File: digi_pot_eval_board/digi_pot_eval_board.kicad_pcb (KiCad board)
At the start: 2 copper layers, 114.3 x 163.2 mm, 85 parts, among them J1 Conn_01x07_Male, J10 Conn_01x02_Male, J11 Conn_01x02_Male, J12 Conn_01x02_Male, J13 Conn_01x06_Male, J14 Conn_01x02_Male, J2 Conn_01x10_Male, J3 USB_B, J4 Conn_01x02_Male, J7 Conn_01x02_Male, J8 DS1013-06S, J9 Conn_01x05_Male, K2 G6K2FYTR5DC, K4 G6K2FYTR5DC, K5 G6K2FYTR5DC, K6 G6K2FYTR5DC, Q1 BSS84, Q2 BSS84, SW1 SW_MEC_5G_LED, U1 DigiPot, U10 6N138, U11 NCP1117ST50T3G, U12 ATmega32U4-AU, U2 DigiPot, U3 DigiPot, U4 DigiPot, U5 DigiPot, U6 DigiPot, U7 DigiPot, U8 ULN2003A, U9 USBLC6-2SC6, Y1 16MHz HC-49SM

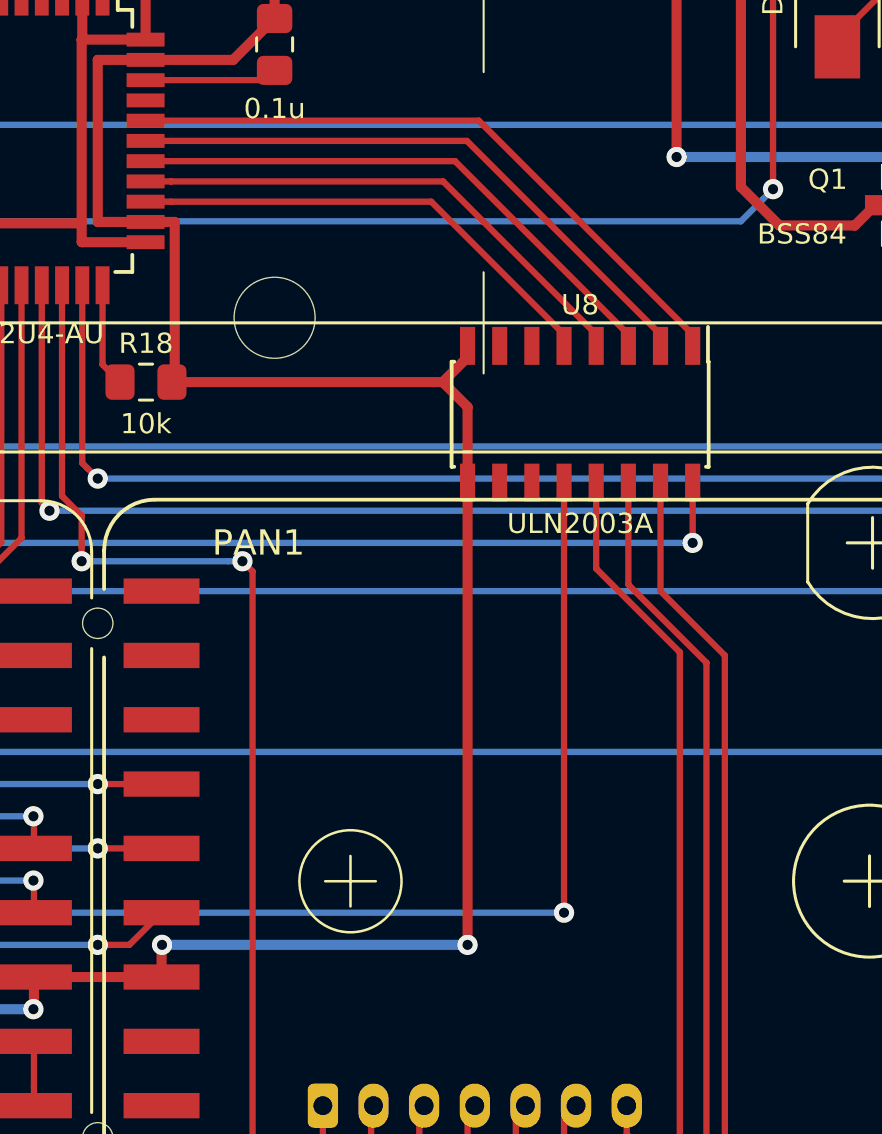
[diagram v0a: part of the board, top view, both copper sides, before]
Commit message: Upgrading KiCad and fixing ULN2003a connection.
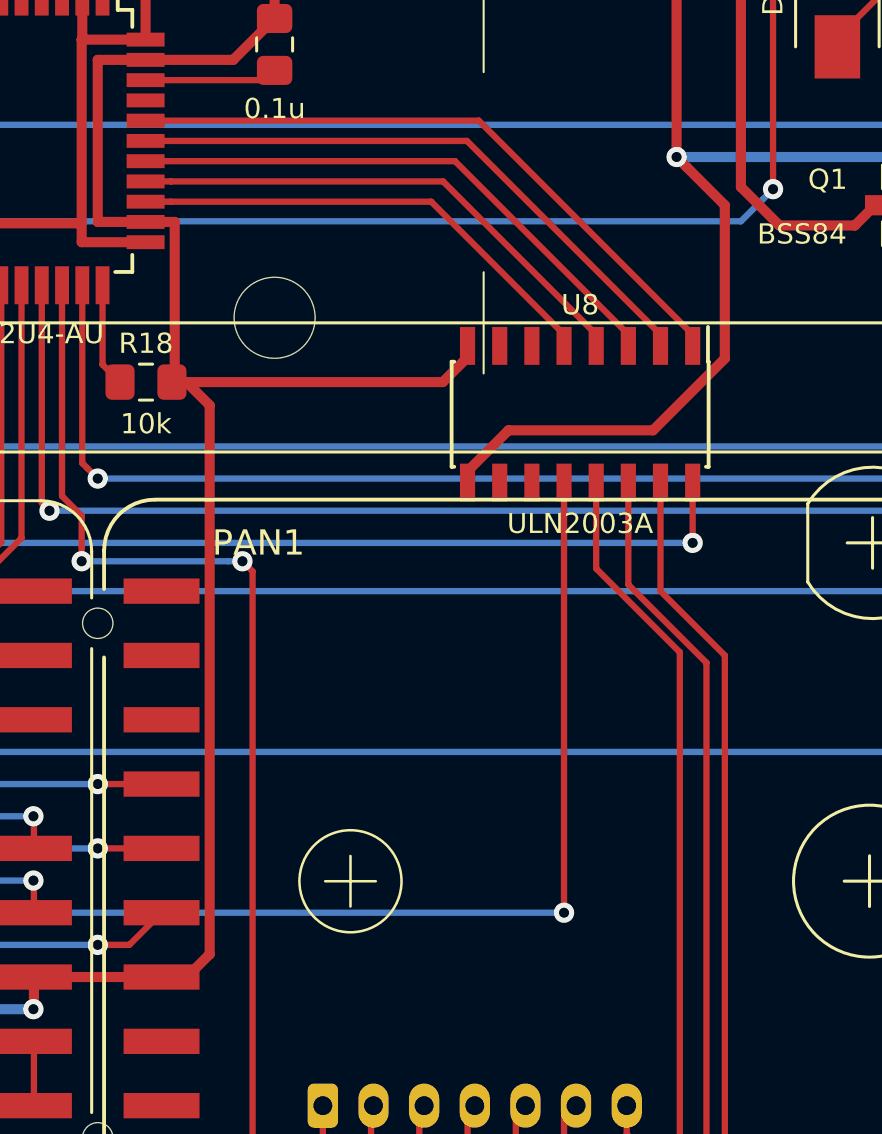
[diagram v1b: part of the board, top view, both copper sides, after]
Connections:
- U8 pad 9: GND -> +5V
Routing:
- net +5V: track 642.4 -> 663.6 mm
- net GND: track 756.2 -> 746.0 mm, vias 28 -> 26
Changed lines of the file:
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@@
-(kicad_pcb (version 20171130) (host pcbnew "(5.0.2-5)-5")
+(kicad_pcb (version 20171130) (host pcbnew "(5.1.5-0-10_14)")
   (general
     (thickness 1.6)
     (drawings 105)
-    (tracks 1145)
+    (tracks 1149)
     (zones 0)
     (modules 85)
@@
   (layers
     (0 F.Cu signal)
-    (31 B.Cu signal hide)
+    (31 B.Cu signal)
     (32 B.Adhes user)
     (33 F.Adhes user)
@@
     (zone_45_only no)
     (trace_min 0.2)
-    (segment_width 0.2)
-    (edge_width 0.15)
     (via_size 0.8)
     (via_drill 0.4)
@@
     (uvia_min_size 0.2)
     (uvia_min_drill 0.1)
+    (edge_width 0.15)
+    (segment_width 0.2)
     (pcb_text_width 0.3)
     (pcb_text_size 1.5 1.5)
@@
       (net 57 "Net-(U8-Pad10)"))
     (pad 9 smd rect (at 2.7 4.445 270) (size 1.5 0.6) (layers F.Cu F.Paste F.Mask)
-      (net 141 GND))
+      (net 3 +5V))
     (pad 8 smd rect (at -2.7 4.445 270) (size 1.5 0.6) (layers F.Cu F.Paste F.Mask)
       (net 141 GND))
@@
   (segment (start 142.76 55.245) (end 139.7 58.305) (width 0.4) (layer F.Cu) (net 3))
   (segment (start 143.51 55.245) (end 142.76 55.245) (width 0.4) (layer F.Cu) (net 3))
-  (segment (start 143.535 71.755) (end 149.835 71.755) (width 0.4) (layer F.Cu) (net 3))
   (segment (start 142.55 118.51) (end 142.875 118.835) (width 0.4) (layer F.Cu) (net 3))
   (via (at 142.875 118.835) (size 0.8) (drill 0.4) (layers F.Cu B.Cu) (net 3))
@@
   (segment (start 159.77 101.6) (end 168.91 92.46) (width 0.4) (layer F.Cu) (net 3))
   (segment (start 158.77 101.6) (end 159.77 101.6) (width 0.4) (layer F.Cu) (net 3))
-  (segment (start 152.155 71.755) (end 158.75 78.35) (width 0.4) (layer F.Cu) (net 3))
-  (segment (start 149.835 71.755) (end 152.155 71.755) (width 0.4) (layer F.Cu) (net 3))
   (segment (start 162.525 78.35) (end 163.83 79.655) (width 0.4) (layer F.Cu) (net 3))
   (segment (start 158.75 78.35) (end 162.525 78.35) (width 0.4) (layer F.Cu) (net 3))
@@
   (segment (start 166.37 82.195) (end 166.37 84.565) (width 0.4) (layer F.Cu) (net 3))
   (segment (start 163.83 79.655) (end 166.37 82.195) (width 0.4) (layer F.Cu) (net 3))
+  (segment (start 149.835 71.755) (end 152.155 71.755) (width 0.4) (layer F.Cu) (net 3))
+  (segment (start 152.155 71.755) (end 158.75 78.35) (width 0.4) (layer F.Cu) (net 3))
+  (segment (start 143.535 71.755) (end 149.835 71.755) (width 0.4) (layer F.Cu) (net 3))
+  (segment (start 123.589999 69.614999) (end 123.19 69.215) (width 0.4) (layer F.Cu) (net 3))
+  (segment (start 125.095 71.12) (end 123.589999 69.614999) (width 0.4) (layer F.Cu) (net 3))
+  (segment (start 125.095 77.175002) (end 125.095 71.12) (width 0.4) (layer F.Cu) (net 3))
+  (segment (start 122.260002 80.01) (end 125.095 77.175002) (width 0.4) (layer F.Cu) (net 3))
+  (segment (start 116.55 80.01) (end 122.260002 80.01) (width 0.4) (layer F.Cu) (net 3))
+  (segment (start 114.935 81.625) (end 116.55 80.01) (width 0.4) (layer F.Cu) (net 3))
+  (segment (start 114.935 82.075) (end 114.935 81.625) (width 0.4) (layer F.Cu) (net 3))
   (segment (start 97.81 148.61) (end 97.79 148.59) (width 0.25) (layer F.Cu) (net 38))
   (via (at 97.79 148.59) (size 0.8) (drill 0.4) (layers F.Cu B.Cu) (net 38))
@@
   (segment (start 97.81 101.6) (end 102.85 101.6) (width 0.4) (layer F.Cu) (net 141))
   (via (at 97.79 102.87) (size 0.8) (drill 0.4) (layers F.Cu B.Cu) (net 141))
-  (segment (start 97.79 102.87) (end 78.105 102.87) (width 0.4) (layer B.Cu) (net 141))
-  (segment (start 97.81 101.6) (end 97.81 102.85) (width 0.4) (layer F.Cu) (net 141))
   (segment (start 97.81 102.85) (end 97.79 102.87) (width 0.4) (layer F.Cu) (net 141))
+  (segment (start 97.81 101.6) (end 97.81 102.85) (width 0.4) (layer F.Cu) (net 141))
+  (segment (start 97.79 102.87) (end 78.105 102.87) (width 0.4) (layer B.Cu) (net 141))
   (via (at 74.929996 102.87) (size 0.8) (drill 0.4) (layers F.Cu B.Cu) (net 141))
-  (segment (start 78.105 102.87) (end 74.929996 102.87) (width 0.4) (layer B.Cu) (net 141))
-  (segment (start 72.37 106.68) (end 74.27 106.68) (width 0.4) (layer F.Cu) (net 141))
-  (segment (start 74.27 106.68) (end 74.929996 106.020004) (width 0.4) (layer F.Cu) (net 141))
-  (segment (start 74.929996 106.020004) (end 74.929996 103.435685) (width 0.4) (layer F.Cu) (net 141))
   (segment (start 74.929996 103.435685) (end 74.929996 102.87) (width 0.4) (layer F.Cu) (net 141))
+  (segment (start 74.929996 106.020004) (end 74.929996 103.435685) (width 0.4) (layer F.Cu) (net 141))
+  (segment (start 74.27 106.68) (end 74.929996 106.020004) (width 0.4) (layer F.Cu) (net 141))
+  (segment (start 72.37 106.68) (end 74.27 106.68) (width 0.4) (layer F.Cu) (net 141))
+  (segment (start 78.105 102.87) (end 74.929996 102.87) (width 0.4) (layer B.Cu) (net 141))
   (segment (start 78.01 98.425) (end 78.01 102.775) (width 0.4) (layer B.Cu) (net 141))
   (segment (start 78.01 102.775) (end 78.105 102.87) (width 0.4) (layer B.Cu) (net 141))
@@
   (segment (start 152.4 135.89) (end 158.75 135.89) (width 0.4) (layer B.Cu) (net 141))
   (segment (start 147.32 135.89) (end 152.4 135.89) (width 0.4) (layer B.Cu) (net 141))
-  (via (at 102.87 100.33) (size 0.8) (drill 0.4) (layers F.Cu B.Cu) (net 141))
-  (segment (start 114.935 100.33) (end 114.935 82.075) (width 0.4) (layer F.Cu) (net 141))
-  (via (at 114.935 100.33) (size 0.8) (drill 0.4) (layers F.Cu B.Cu) (net 141))
-  (segment (start 102.87 100.33) (end 114.935 100.33) (width 0.4) (layer B.Cu) (net 141))
-  (segment (start 102.85 101.6) (end 102.85 100.35) (width 0.4) (layer F.Cu) (net 141))
-  (segment (start 102.85 100.35) (end 102.87 100.33) (width 0.4) (layer F.Cu) (net 141))
   (segment (start 76.445 63.754) (end 76.445 64.554) (width 0.4) (layer F.Cu) (net 141))
   (segment (start 86.03 66.98) (end 85.725 66.675) (width 0.4) (layer F.Cu) (net 141))
@@
   (segment (start 113.955 78.105) (end 114.935 77.125) (width 0.4) (layer F.Cu) (net 141))
   (segment (start 103.26 78.105) (end 113.955 78.105) (width 0.4) (layer F.Cu) (net 141))
-  (segment (start 114.935 79.085) (end 113.955 78.105) (width 0.4) (layer F.Cu) (net 141))
-  (segment (start 114.935 82.075) (end 114.935 79.085) (width 0.4) (layer F.Cu) (net 141))
   (segment (start 125.85 48.77) (end 125.85 48.895) (width 0.4) (layer B.Cu) (net 141))
   (segment (start 124.59999 47.51999) (end 125.85 48.77) (width 0.4) (layer B.Cu) (net 141))
@@
   (segment (start 125.85 48.77) (end 127.10001 47.51999) (width 0.4) (layer F.Cu) (net 141))
   (segment (start 125.85 48.895) (end 125.85 48.77) (width 0.4) (layer F.Cu) (net 141))
-  (segment (start 147.565 62.865) (end 147.955 63.255) (width 0.6) (layer F.Cu) (net 141) (status 1000000))
-  (segment (start 143.51 62.865) (end 147.565 62.865) (width 0.6) (layer F.Cu) (net 141) (status 1000000))
+  (segment (start 147.565 62.865) (end 147.955 63.255) (width 0.6) (layer F.Cu) (net 141))
+  (segment (start 143.51 62.865) (end 147.565 62.865) (width 0.6) (layer F.Cu) (net 141))
   (segment (start 149.225 63.255) (end 150.495 61.985) (width 0.6) (layer F.Cu) (net 141))
   (segment (start 147.955 63.255) (end 149.225 63.255) (width 0.6) (layer F.Cu) (net 141))
+  (segment (start 104.750001 79.020001) (end 104.75 100.7) (width 0.4) (layer F.Cu) (net 141))
+  (segment (start 103.85 101.6) (end 102.85 101.6) (width 0.4) (layer F.Cu) (net 141))
+  (segment (start 103.835 78.105) (end 104.750001 79.020001) (width 0.4) (layer F.Cu) (net 141))
+  (segment (start 104.75 100.7) (end 103.85 101.6) (width 0.4) (layer F.Cu) (net 141))
+  (segment (start 103.26 78.105) (end 103.835 78.105) (width 0.4) (layer F.Cu) (net 141))
   (via (at 90.805 63.5) (size 0.8) (drill 0.4) (layers F.Cu B.Cu) (net 142))
   (segment (start 90.82 63.515) (end 90.805 63.5) (width 0.25) (layer F.Cu) (net 142))

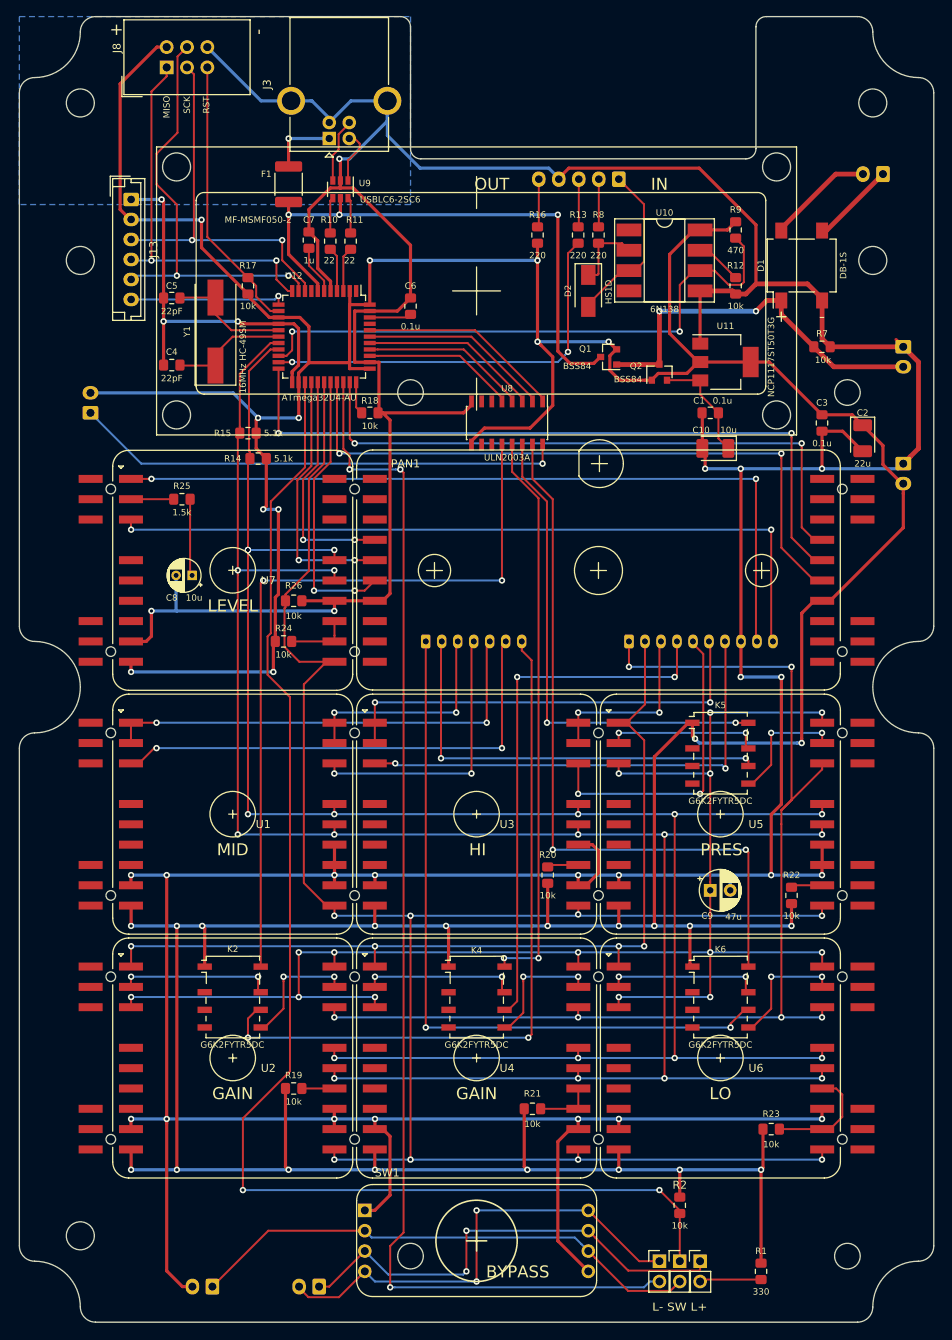
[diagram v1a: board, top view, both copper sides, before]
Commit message: digi_pot_eval_board: switch to KiCad 7.0
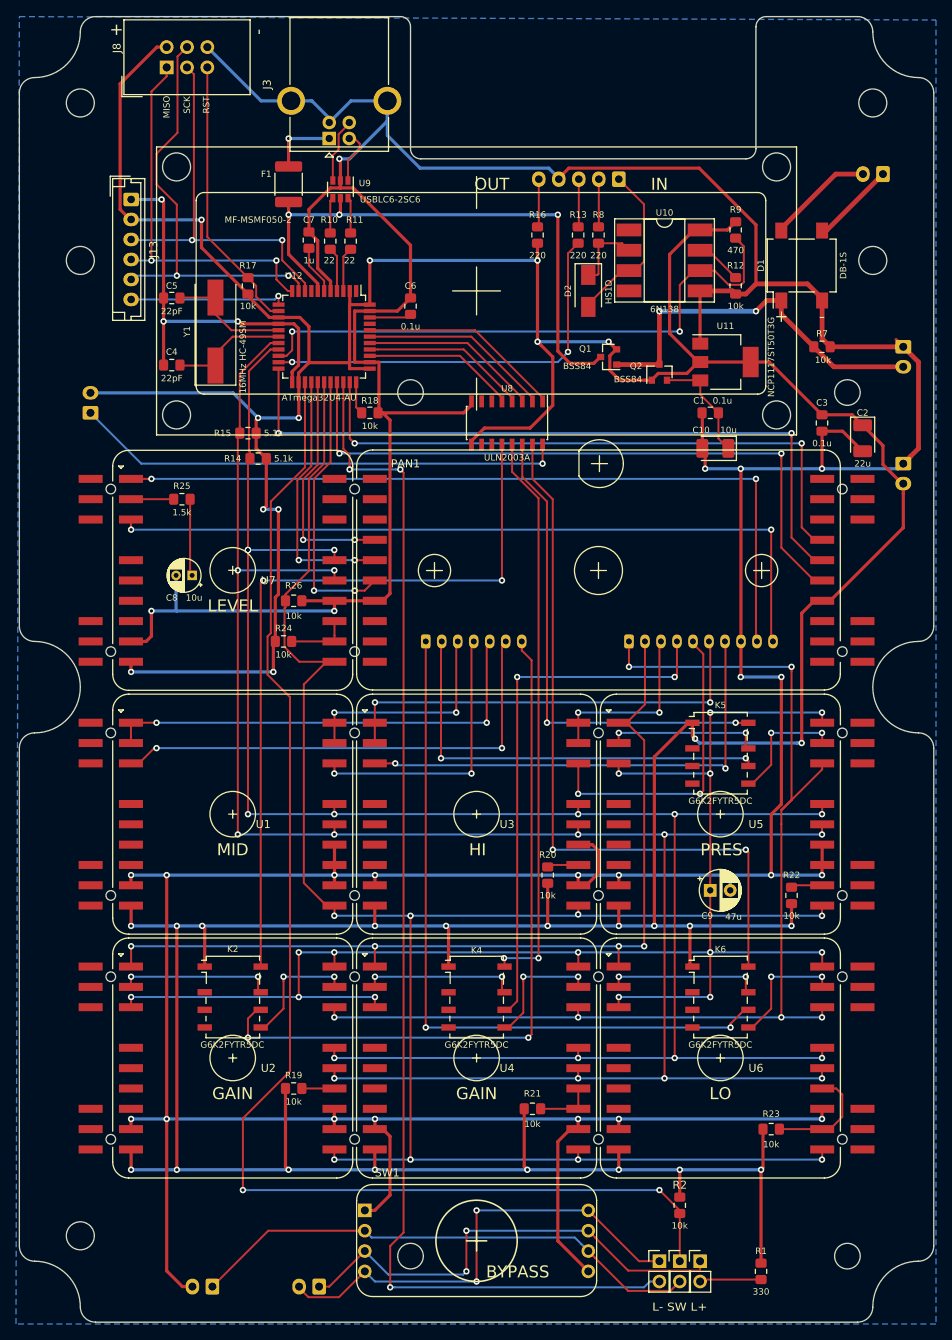
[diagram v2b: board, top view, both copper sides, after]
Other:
- net class Default removed
- net class Extra Thick removed
- net class Thick removed
